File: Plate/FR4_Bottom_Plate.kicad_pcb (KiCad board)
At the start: 2 copper layers, 139.1 x 107.7 mm, 5 parts

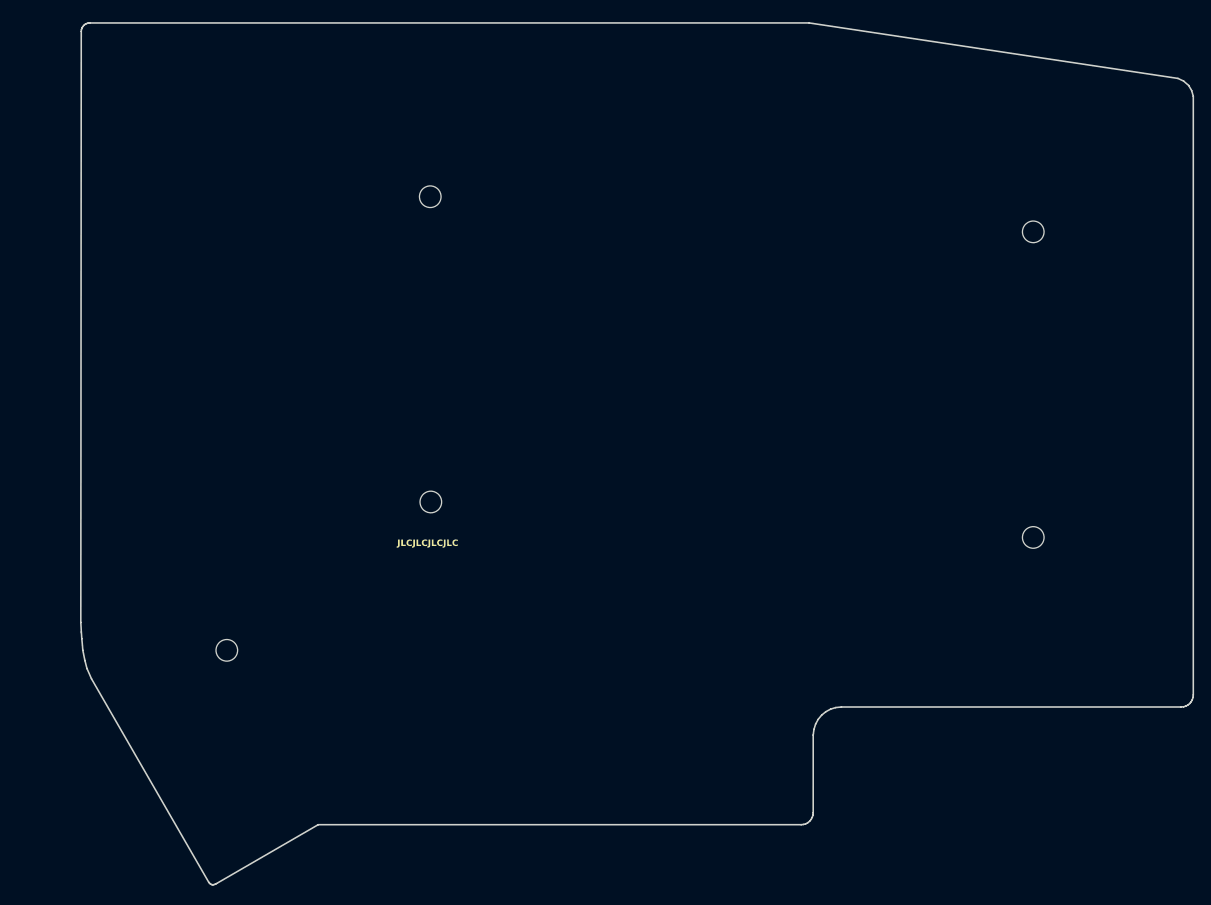
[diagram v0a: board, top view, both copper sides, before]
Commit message: Revert "Merge pull request #53 from TweetyDaBird/release"
This reverts commit d5395b9879702c31b6de7b44cd45c4487da02165, reversing
changes made to 721366541e1b3daa08e8a27e832954bcb38f5212.

# Conflicts:
#	.gitignore
#	Lotus 58 Classic/v1.26/Lotus58_Glow_126.kicad_pcb
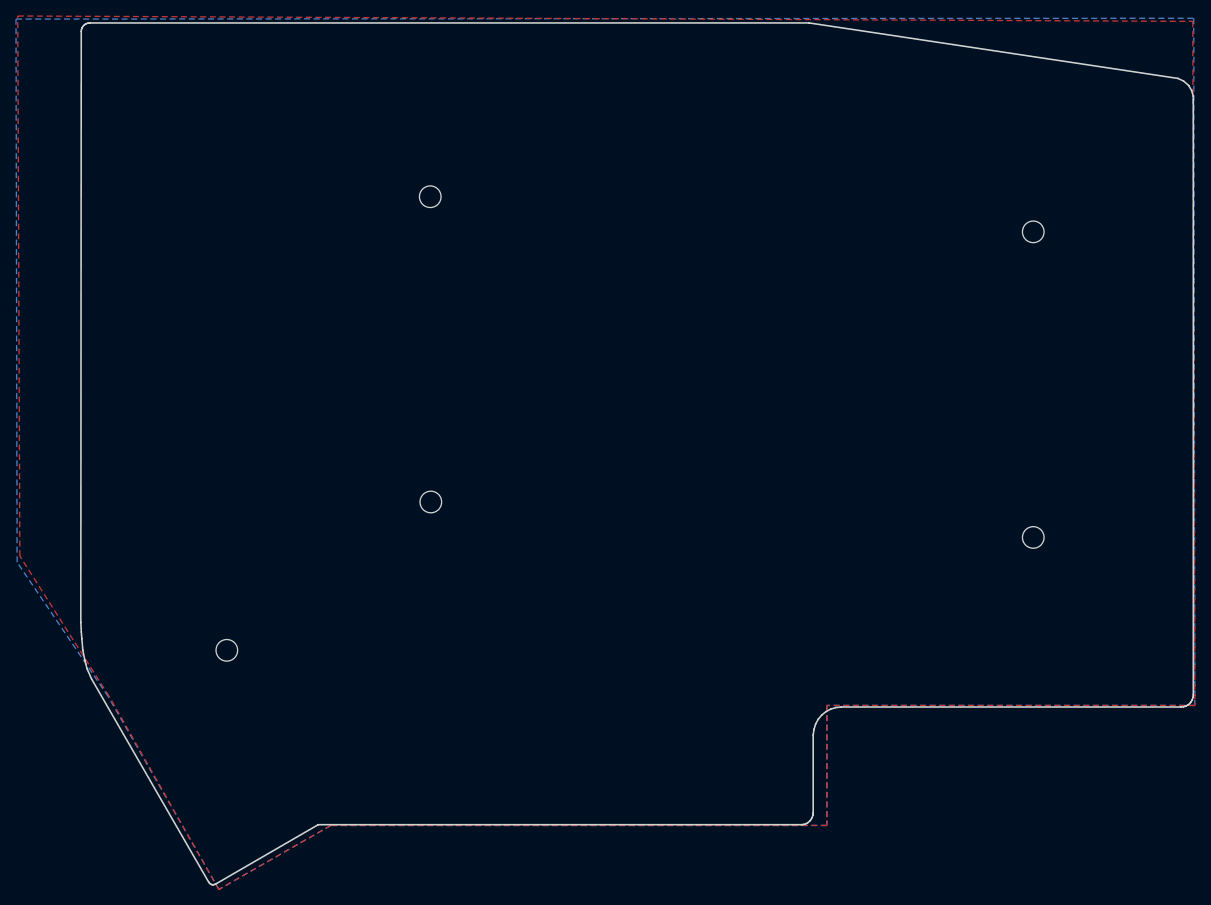
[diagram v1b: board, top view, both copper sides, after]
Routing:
- added copper zone on B.Cu, net (none)
- added copper zone on F.Cu, net (none)
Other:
- board text removed: "JLCJLCJLCJLC"

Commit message: Updated plates
Plates now have no copper layer, both preparing for wireless, and to avoid scratches/shorting, if OLED etc. is not soldered with flat pads.
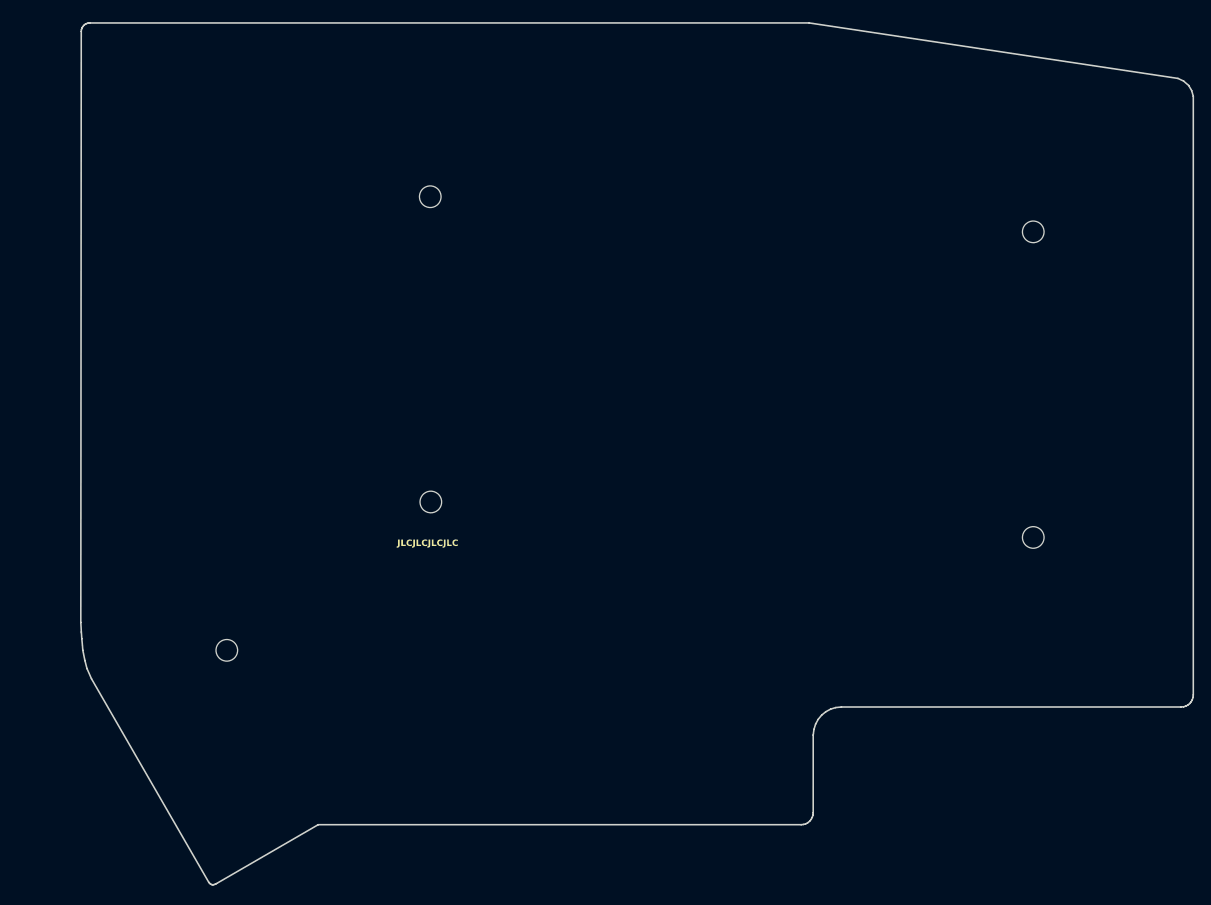
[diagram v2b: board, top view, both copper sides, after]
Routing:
- removed copper zone on B.Cu, net (none)
- removed copper zone on F.Cu, net (none)
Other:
- board text added: "JLCJLCJLCJLC"
